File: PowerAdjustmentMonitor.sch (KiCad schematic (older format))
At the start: 44 parts, among them K2 CONN_3, K3 CONN_3, P6 CONN_1, P7 CONN_1, U11 LM317T, U6 LM337T, U8 LM337T, U9 LM317T

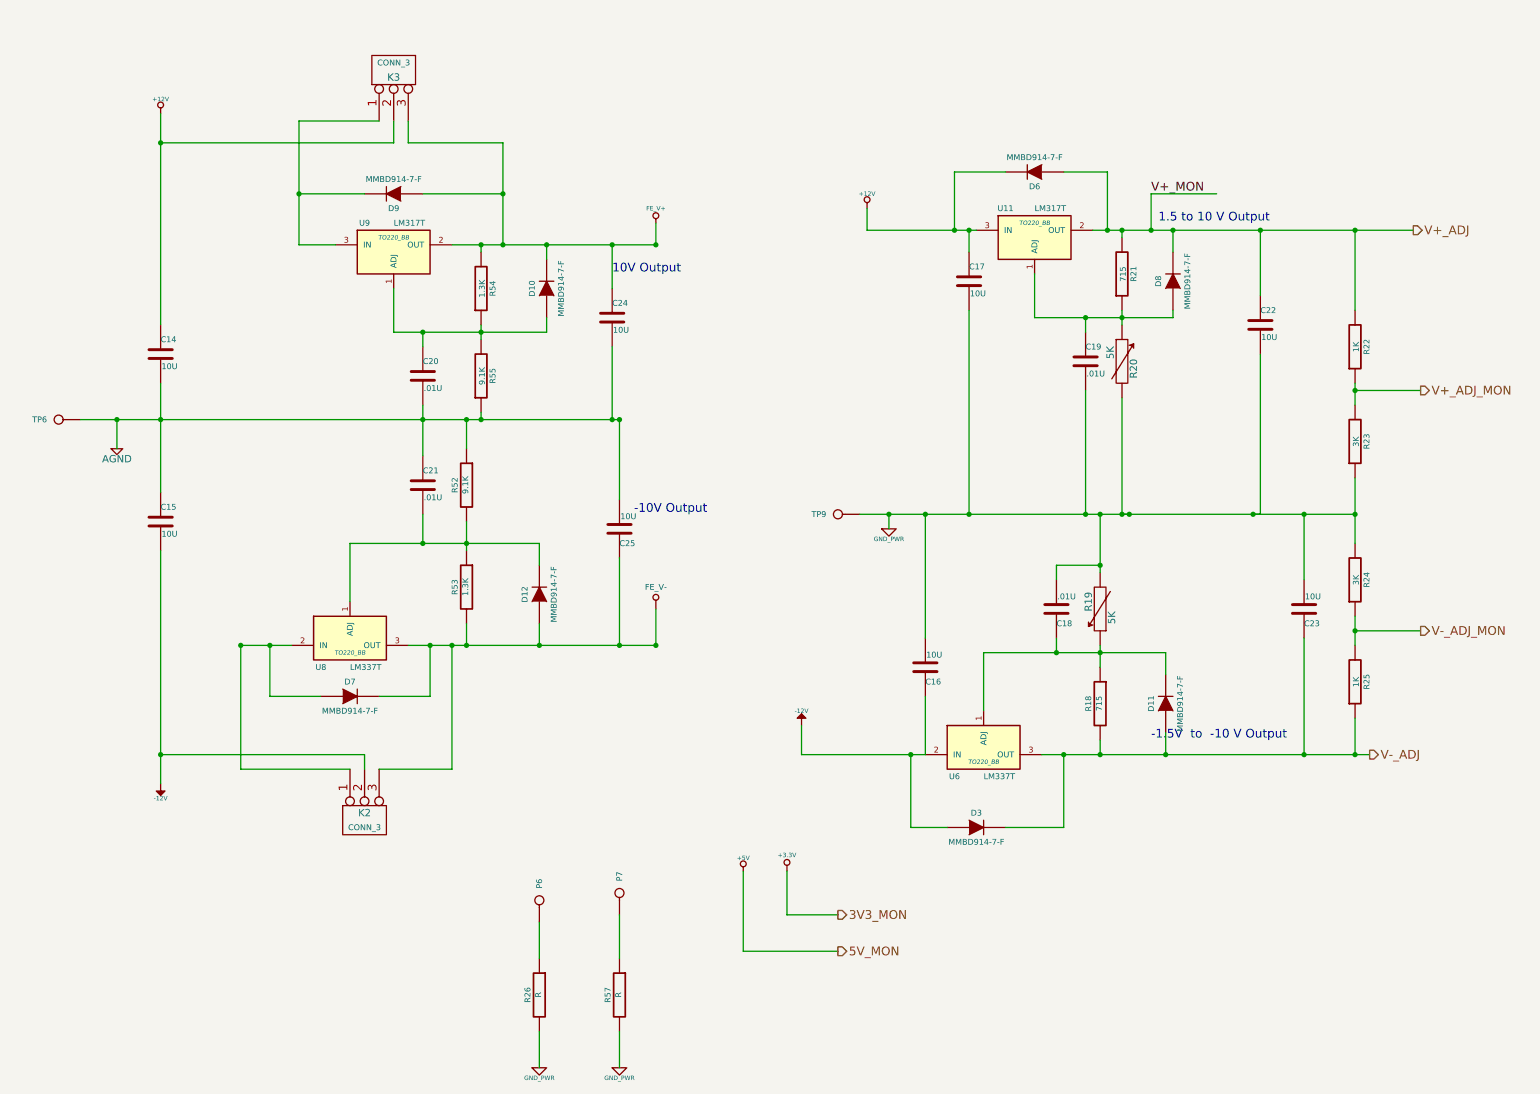
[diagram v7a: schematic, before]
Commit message: Added the schematic and BOM changes back in after hard reset
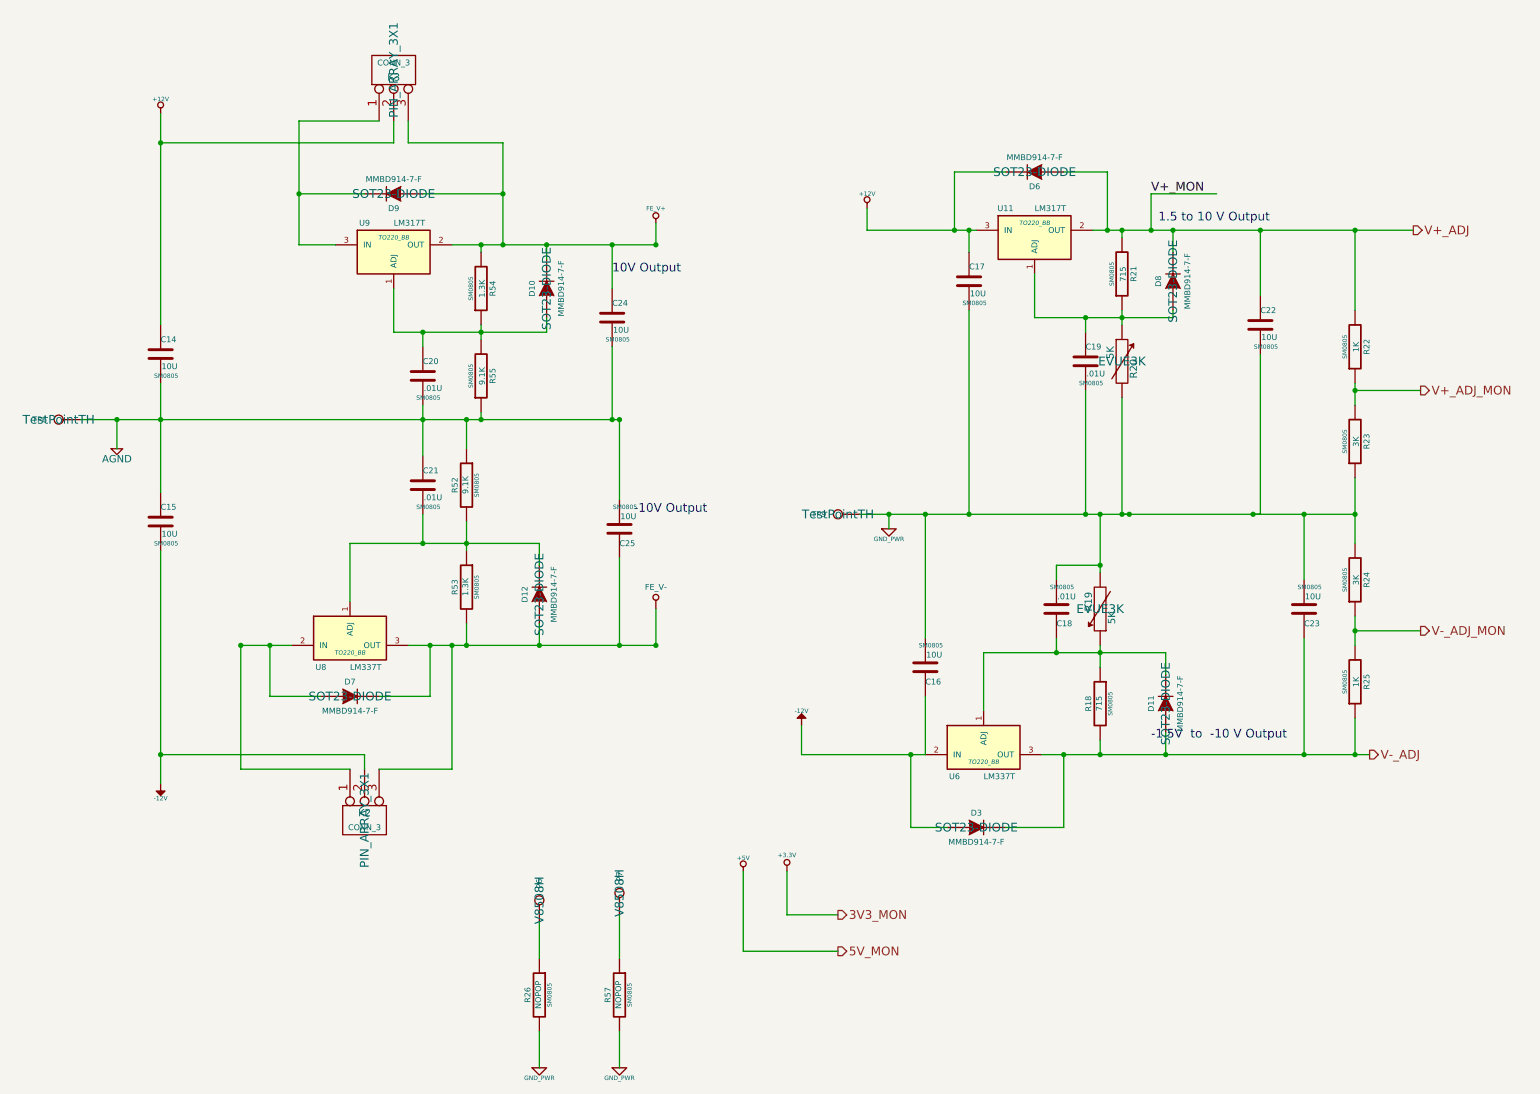
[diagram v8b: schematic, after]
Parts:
- C14, C15, C16, C17, C18, C19, C20, C21, C22, C23, C24, C25, R18, R21, R22, R23, R24, R25, R52, R53, R54, R55: footprint ~ -> SM0805
- D10, D11, D12, D3, D6, D7, D8, D9: footprint ~ -> SOT23-DIODE
- K2, K3: footprint (none) -> PIN_ARRAY_3X1
- P6, P7: footprint (none) -> V8508H
- R19, R20: footprint ~ -> EVUE3K
- R26, R57: value R -> NOPOP; footprint ~ -> SM0805
- TP6, TP9: footprint (none) -> TestPointTH
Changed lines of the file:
@@
-EESchema Schematic File Version 2  date 4/16/2014 11:04:06 PM
+EESchema Schematic File Version 2  date 4/18/2014 9:49:53 PM
 LIBS:power
 LIBS:device
@@
 Sheet 5 9
 Title ""
-Date "17 apr 2014"
+Date "19 apr 2014"
 Rev ""
 Comp ""
@@
 F 0 "R21" V 8230 2150 40  0000 C CNN
 F 1 "715" V 8157 2151 40  0000 C CNN
-F 2 "~" V 8080 2150 30  0000 C CNN
+F 2 "SM0805" V 8080 2150 30  0000 C CNN
 F 3 "~" H 8150 2150 30  0000 C CNN
 	1    8150 2150
@@
 F 0 "R22" V 9830 2650 40  0000 C CNN
 F 1 "1K" V 9757 2651 40  0000 C CNN
-F 2 "~" V 9680 2650 30  0000 C CNN
+F 2 "SM0805" V 9680 2650 30  0000 C CNN
 F 3 "~" H 9750 2650 30  0000 C CNN
 	1    9750 2650
@@
 F 0 "R23" V 9830 3300 40  0000 C CNN
 F 1 "3K" V 9757 3301 40  0000 C CNN
-F 2 "~" V 9680 3300 30  0000 C CNN
+F 2 "SM0805" V 9680 3300 30  0000 C CNN
 F 3 "~" H 9750 3300 30  0000 C CNN
 	1    9750 3300
@@
 F 0 "R24" V 9830 4250 40  0000 C CNN
 F 1 "3K" V 9757 4251 40  0000 C CNN
-F 2 "~" V 9680 4250 30  0000 C CNN
+F 2 "SM0805" V 9680 4250 30  0000 C CNN
 F 3 "~" H 9750 4250 30  0000 C CNN
 	1    9750 4250
@@
 F 0 "R25" V 9830 4950 40  0000 C CNN
 F 1 "1K" V 9757 4951 40  0000 C CNN
-F 2 "~" V 9680 4950 30  0000 C CNN
+F 2 "SM0805" V 9680 4950 30  0000 C CNN
 F 3 "~" H 9750 4950 30  0000 C CNN
 	1    9750 4950
@@
 F 0 "R20" V 8230 2700 50  0000 C CNN
 F 1 "5K" V 8070 2810 50  0000 C CNN
-F 2 "~" H 8150 2750 60  0000 C CNN
+F 2 "EVUE3K" H 8150 2750 60  0000 C CNN
 F 3 "~" H 8150 2750 60  0000 C CNN
 	1    8150 2750
@@
 F 0 "R55" V 3830 2850 40  0000 C CNN
 F 1 "9.1K" V 3757 2851 40  0000 C CNN
-F 2 "~" V 3680 2850 30  0000 C CNN
+F 2 "SM0805" V 3680 2850 30  0000 C CNN
 F 3 "~" H 3750 2850 30  0000 C CNN
 	1    3750 2850
@@
 F 0 "R54" V 3830 2250 40  0000 C CNN
 F 1 "1.3K" V 3757 2251 40  0000 C CNN
-F 2 "~" V 3680 2250 30  0000 C CNN
+F 2 "SM0805" V 3680 2250 30  0000 C CNN
 F 3 "~" H 3750 2250 30  0000 C CNN
 	1    3750 2250
@@
 F 0 "R52" V 3730 3600 40  0000 C CNN
 F 1 "9.1K" V 3657 3601 40  0000 C CNN
-F 2 "~" V 3580 3600 30  0000 C CNN
+F 2 "SM0805" V 3580 3600 30  0000 C CNN
 F 3 "~" H 3650 3600 30  0000 C CNN
 	1    3650 3600
@@
 F 0 "R53" V 3730 4300 40  0000 C CNN
 F 1 "1.3K" V 3657 4301 40  0000 C CNN
-F 2 "~" V 3580 4300 30  0000 C CNN
+F 2 "SM0805" V 3580 4300 30  0000 C CNN
 F 3 "~" H 3650 4300 30  0000 C CNN
 	1    3650 4300
@@
 F 0 "R18" V 8080 5100 40  0000 C CNN
 F 1 "715" V 8007 5101 40  0000 C CNN
-F 2 "~" V 7930 5100 30  0000 C CNN
+F 2 "SM0805" V 7930 5100 30  0000 C CNN
 F 3 "~" H 8000 5100 30  0000 C CNN
 	1    8000 5100
@@
 F 0 "R19" V 8080 4400 50  0000 C CNN
 F 1 "5K" V 7920 4510 50  0000 C CNN
-F 2 "~" H 8000 4450 60  0000 C CNN
+F 2 "EVUE3K" H 8000 4450 60  0000 C CNN
 F 3 "~" H 8000 4450 60  0000 C CNN
 	1    8000 4450
@@
 F 0 "C22" H 9100 2600 40  0000 L CNN
 F 1 "10U" H 9106 2415 40  0000 L CNN
-F 2 "~" H 9138 2350 30  0000 C CNN
+F 2 "SM0805" H 9138 2350 30  0000 C CNN
 F 3 "~" H 9100 2500 60  0000 C CNN
 	1    9100 2500
@@
 F 0 "C25" H 4700 4000 40  0000 L CNN
 F 1 "10U" H 4706 3815 40  0000 L CNN
-F 2 "~" H 4738 3750 30  0000 C CNN
+F 2 "SM0805" H 4738 3750 30  0000 C CNN
 F 3 "~" H 4700 3900 60  0000 C CNN
 	1    4700 3900
@@
 F 0 "C23" H 9400 4550 40  0000 L CNN
 F 1 "10U" H 9406 4365 40  0000 L CNN
-F 2 "~" H 9438 4300 30  0000 C CNN
+F 2 "SM0805" H 9438 4300 30  0000 C CNN
 F 3 "~" H 9400 4450 60  0000 C CNN
 	1    9400 4450
@@
 F 0 "C16" H 6800 4950 40  0000 L CNN
 F 1 "10U" H 6806 4765 40  0000 L CNN
-F 2 "~" H 6838 4700 30  0000 C CNN
+F 2 "SM0805" H 6838 4700 30  0000 C CNN
 F 3 "~" H 6800 4850 60  0000 C CNN
 	1    6800 4850
@@
 F 0 "C15" H 1550 3950 40  0000 L CNN
 F 1 "10U" H 1556 3765 40  0000 L CNN
-F 2 "~" H 1588 3700 30  0000 C CNN
+F 2 "SM0805" H 1588 3700 30  0000 C CNN
 F 3 "~" H 1550 3850 60  0000 C CNN
 	1    1550 3850
@@
 F 0 "C14" H 1550 2800 40  0000 L CNN
 F 1 "10U" H 1556 2615 40  0000 L CNN
-F 2 "~" H 1588 2550 30  0000 C CNN
+F 2 "SM0805" H 1588 2550 30  0000 C CNN
 F 3 "~" H 1550 2700 60  0000 C CNN
 	1    1550 2700
@@
 F 0 "C17" H 7100 2300 40  0000 L CNN
 F 1 "10U" H 7106 2115 40  0000 L CNN
-F 2 "~" H 7138 2050 30  0000 C CNN
+F 2 "SM0805" H 7138 2050 30  0000 C CNN
 F 3 "~" H 7100 2200 60  0000 C CNN
 	1    7100 2200
@@
 F 0 "C21" H 3350 3700 40  0000 L CNN
 F 1 ".01U" H 3356 3515 40  0000 L CNN
-F 2 "~" H 3388 3450 30  0000 C CNN
+F 2 "SM0805" H 3388 3450 30  0000 C CNN
 F 3 "~" H 3350 3600 60  0000 C CNN
 	1    3350 3600
@@
 F 0 "C20" H 3350 2950 40  0000 L CNN
 F 1 ".01U" H 3356 2765 40  0000 L CNN
-F 2 "~" H 3388 2700 30  0000 C CNN
+F 2 "SM0805" H 3388 2700 30  0000 C CNN
 F 3 "~" H 3350 2850 60  0000 C CNN
 	1    3350 2850
@@
 F 0 "C19" H 7900 2850 40  0000 L CNN
 F 1 ".01U" H 7906 2665 40  0000 L CNN
-F 2 "~" H 7938 2600 30  0000 C CNN
+F 2 "SM0805" H 7938 2600 30  0000 C CNN
 F 3 "~" H 7900 2750 60  0000 C CNN
 	1    7900 2750
@@
 F 0 "C18" H 7700 4550 40  0000 L CNN
 F 1 ".01U" H 7706 4365 40  0000 L CNN
-F 2 "~" H 7738 4300 30  0000 C CNN
+F 2 "SM0805" H 7738 4300 30  0000 C CNN
 F 3 "~" H 7700 4450 60  0000 C CNN
 	1    7700 4450
@@
 F 0 "C24" H 4650 2550 40  0000 L CNN
 F 1 "10U" H 4656 2365 40  0000 L CNN
-F 2 "~" H 4688 2300 30  0000 C CNN
+F 2 "SM0805" H 4688 2300 30  0000 C CNN
 F 3 "~" H 4650 2450 60  0000 C CNN
 	1    4650 2450
@@
 F 0 "D10" H 4200 2350 40  0000 C CNN
 F 1 "MMBD914-7-F" H 4200 2150 40  0000 C CNN
-F 2 "~" H 4200 2250 60  0000 C CNN
+F 2 "SOT23-DIODE" H 4200 2250 60  0000 C CNN
 F 3 "~" H 4200 2250 60  0000 C CNN
 	1    4200 2250
@@
 F 0 "D8" H 8500 2300 40  0000 C CNN
 F 1 "MMBD914-7-F" H 8500 2100 40  0000 C CNN
-F 2 "~" H 8500 2200 60  0000 C CNN
+F 2 "SOT23-DIODE" H 8500 2200 60  0000 C CNN
 F 3 "~" H 8500 2200 60  0000 C CNN
 	1    8500 2200
@@
 F 0 "D6" H 7550 1550 40  0000 C CNN
 F 1 "MMBD914-7-F" H 7550 1350 40  0000 C CNN
-F 2 "~" H 7550 1450 60  0000 C CNN
+F 2 "SOT23-DIODE" H 7550 1450 60  0000 C CNN
 F 3 "~" H 7550 1450 60  0000 C CNN
 	1    7550 1450
@@
 F 0 "D9" H 3150 1700 40  0000 C CNN
 F 1 "MMBD914-7-F" H 3150 1500 40  0000 C CNN
-F 2 "~" H 3150 1600 60  0000 C CNN
+F 2 "SOT23-DIODE" H 3150 1600 60  0000 C CNN
 F 3 "~" H 3150 1600 60  0000 C CNN
 	1    3150 1600
@@
 F 0 "D12" H 4150 4450 40  0000 C CNN
 F 1 "MMBD914-7-F" H 4150 4250 40  0000 C CNN
-F 2 "~" H 4150 4350 60  0000 C CNN
+F 2 "SOT23-DIODE" H 4150 4350 60  0000 C CNN
 F 3 "~" H 4150 4350 60  0000 C CNN
 	1    4150 4350
@@
 F 0 "D7" H 2850 5150 40  0000 C CNN
 F 1 "MMBD914-7-F" H 2850 4950 40  0000 C CNN
-F 2 "~" H 2850 5050 60  0000 C CNN
+F 2 "SOT23-DIODE" H 2850 5050 60  0000 C CNN
 F 3 "~" H 2850 5050 60  0000 C CNN
 	1    2850 5050
@@
 F 0 "D3" H 7150 6050 40  0000 C CNN
 F 1 "MMBD914-7-F" H 7150 5850 40  0000 C CNN
-F 2 "~" H 7150 5950 60  0000 C CNN
+F 2 "SOT23-DIODE" H 7150 5950 60  0000 C CNN
 F 3 "~" H 7150 5950 60  0000 C CNN
 	1    7150 5950
@@
 F 0 "D11" H 8450 5200 40  0000 C CNN
 F 1 "MMBD914-7-F" H 8450 5000 40  0000 C CNN
-F 2 "~" H 8450 5100 60  0000 C CNN
+F 2 "SOT23-DIODE" H 8450 5100 60  0000 C CNN
 F 3 "~" H 8450 5100 60  0000 C CNN
 	1    8450 5100
@@
 P 4150 7100
 F 0 "R26" V 4230 7100 40  0000 C CNN
-F 1 "R" V 4157 7101 40  0000 C CNN
-F 2 "~" V 4080 7100 30  0000 C CNN
+F 1 "NOPOP" V 4157 7101 40  0000 C CNN
+F 2 "SM0805" V 4080 7100 30  0000 C CNN
 F 3 "~" H 4150 7100 30  0000 C CNN
 	1    4150 7100
@@
 P 4700 7100
 F 0 "R57" V 4780 7100 40  0000 C CNN
-F 1 "R" V 4707 7101 40  0000 C CNN
-F 2 "~" V 4630 7100 30  0000 C CNN
+F 1 "NOPOP" V 4707 7101 40  0000 C CNN
+F 2 "SM0805" V 4630 7100 30  0000 C CNN
 F 3 "~" H 4700 7100 30  0000 C CNN
 	1    4700 7100
@@
 F 0 "P7" H 4780 6400 40  0000 L CNN
 F 1 "CONN_1" H 4700 6455 30  0001 C CNN
-F 2 "" H 4700 6400 60  0000 C CNN
+F 2 "V8508H" H 4700 6400 60  0000 C CNN
 F 3 "" H 4700 6400 60  0000 C CNN
 	1    4700 6400
@@
 F 0 "P6" H 4230 6450 40  0000 L CNN
 F 1 "CONN_1" H 4150 6505 30  0001 C CNN
-F 2 "" H 4150 6450 60  0000 C CNN
+F 2 "V8508H" H 4150 6450 60  0000 C CNN
 F 3 "" H 4150 6450 60  0000 C CNN
 	1    4150 6450
@@
 F 0 "TP9" H 6280 3800 40  0000 L CNN
 F 1 "GND_PWR" H 6200 3855 30  0001 C CNN
-F 2 "" H 6200 3800 60  0000 C CNN
+F 2 "TestPointTH" H 6200 3800 60  0000 C CNN
 F 3 "" H 6200 3800 60  0000 C CNN
 	1    6200 3800
@@
 F 0 "TP6" H 930 3150 40  0000 L CNN
 F 1 "AGND" H 850 3205 30  0001 C CNN
-F 2 "" H 850 3150 60  0000 C CNN
+F 2 "TestPointTH" H 850 3150 60  0000 C CNN
 F 3 "" H 850 3150 60  0000 C CNN
 	1    850  3150
@@
 F 0 "K3" V 3100 750 50  0000 C CNN
 F 1 "CONN_3" V 3200 750 40  0000 C CNN
-F 2 "" H 3150 750 60  0000 C CNN
+F 2 "PIN_ARRAY_3X1" H 3150 750 60  0000 C CNN
 F 3 "" H 3150 750 60  0000 C CNN
 	1    3150 750
@@
 F 0 "K2" V 2900 5900 50  0000 C CNN
 F 1 "CONN_3" V 3000 5900 40  0000 C CNN
-F 2 "" H 2950 5900 60  0000 C CNN
+F 2 "PIN_ARRAY_3X1" H 2950 5900 60  0000 C CNN
 F 3 "" H 2950 5900 60  0000 C CNN
 	1    2950 5900
